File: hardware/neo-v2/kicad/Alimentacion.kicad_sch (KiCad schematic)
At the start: 64 parts, among them Q201 FS8205A, Q202 FS8205A, Q203 CSD25402Q3A, SW201 MSK-22D18G3, U201 TPS2121RUXR, U202 TPS61022RWUT, U203 BQ25170DSGR, U204 MAX17048G+T10, U205 DW01A

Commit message: NEO v2 fase 4: colocación y plan de layout
- PCB generado por script (tools/update_pcb.py) desde el PCB original de
  Nabu Casa y la netlist: contorno 84 x 89 mm con franja superior para
  batería y potencia, huellas retiradas y nuevas, zonas ampliadas,
  colocación de los bloques propios y de los puntos de prueba.
- Unión de fuentes rehecha: TPS2121 de entrada única abajo (sitio de U13)
  y LM66200 como diodo ideal en la franja, unidos por el plano +5V;
  elevador a 4,59 V. Cálculos actualizados.
- Retirados TP213 y TP221 (sin sitio); valor/DNP sincronizados.
- Huellas heredadas exportadas a kicad/lib/inherited (ERC sin avisos de
  enlace de huella).
- Paridad PCB/esquemático sin incidencias; DRC sin errores nuevos.
- docs/fase4-colocacion.md, renders, CHANGES y README.

Co-Authored-By: Claude Opus 5.5 <noreply@anthropic.com>
Claude-Session: https://claude.ai/code/session_01UWwWJAyCeb1aBHbGbkDaMx
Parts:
- removed R216, R218: 100k, Resistor_SMD:R_0402_1005Metric, symbol Device:R
- removed R217: 36.5k, Resistor_SMD:R_0402_1005Metric, symbol Device:R
- removed R219: 31.6k, Resistor_SMD:R_0402_1005Metric, symbol Device:R
- removed R223: 10k, Resistor_SMD:R_0402_1005Metric, symbol Device:R
- removed R224: 2.2M, Resistor_SMD:R_0402_1005Metric, symbol Device:R
- removed TP212: MUX_ST, TestPoint:TestPoint_Pad_D1.0mm, symbol Connector:TestPoint
- removed TP213: MUX_OV1, TestPoint:TestPoint_Pad_D1.0mm, symbol Connector:TestPoint
- added C218: 22uF 25V, Capacitor_SMD:C_0805_2012Metric, symbol Device:C
- added C219: 100nF, Capacitor_SMD:C_0402_1005Metric, symbol Device:C
- added U206: LM66200DRLR, Package_TO_SOT_SMD:SOT-583-8, symbol NEO_v2:LM66200
- R209: value 732k -> 665k; LCSC C27016 -> C56583
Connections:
- net MUX_CP2 is gone; now on net GND: U201.3 (CP2)
- net MUX_PR1 is gone; now on net GND: U201.6 (PR1)
- net +5V: now also C218.1, C219.1, U206.2 (VOUT), U206.7 (VOUT)
- net BOOST_5V: now also U206.3 (VIN1); no longer U201.2 (IN2)
- net GND: now also U201.2 (IN2), C218.2, C219.2, U206.1 (GND), U206.4 (~{ON}), U206.5 (GND), U206.6 (VIN2)
- net MUX_ST: no longer names the net of U201.9 (ST)
- no-connect marks 2 -> 4
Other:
- note added: "ELEVADOR TPS61022 (SLVSDX7D, fase 2 §4.2) VOUT = 0,6 V x (1 + 665k/100k) = 4,59 V (fase 4: por debajo de USB para el diodo ideal U206). MODE alto = PWM forzado (R211 0 Ohm; R212 DNP = PFM). L201 1 uH: IL pico 5,26 A a 2,7 V y 2 A < Isat 12 A; valle 3,44 A < ILIM mín. 6,5 A. COUT 3x22 uF (~30 uF efectivos): eq. 8 pide 21,6 uF para 50 mV pp. R214: puente 1206 de 0 Ohm; huella prevista para ferrita 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"
- note added: "UNIÓN DE FUENTES (fase 4, docs/fase4-colocacion.md §2). Sustituye al multiplexor único de la fase 2: entre la franja (batería) y el sitio de U13 (USB) no cabe una pista de 1,5-2 A en la placa heredada. U201 abajo: VBUS -> +5V, ILIM 44,2 k (2,0-3,0 A), OV1 43,2k/10k (5,64 V), SS 100 nF. Entrada única. U206 arriba: BOOST_5V (4,59 V) -> +5V. Con USB, +5V (~4,8-5,0 V) > BOOST_5V + 70 mV: bloquea. Sin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"
- note removed: "ELEVADOR TPS61022 (SLVSDX7D, fase 2 §4.2) VOUT = 0,6 V x (1 + 732k/100k) = 4,992 V. MODE alto = PWM forzado (R211 0 Ohm; R212 DNP = PFM). L201 1 uH: IL pico 5,26 A a 2,7 V y 2 A < Isat 12 A; valle 3,44 A < ILIM mín. 6,5 A. COUT 3x22 uF (~30 uF efectivos): eq. 8 pide 21,6 uF para 50 mV pp. R214: puente 1206 de 0 Ohm; huella prevista para ferrita si la medida lo pide. INTERRUPTOR SW201 (señal): OFF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"
- note removed: "MULTIPLEXOR TPS2121 (SLVSEA3F, fase 2 §4.1). Sustituye a U13 (SGM2594B). Modo XREF: IN1 (VBUS) si PR1 > CP2. CP2 = 4,992 x 31,6/131,6 = 1,199 V (> VREF máx. 1,10 V). PR1 100k/36,5k + 2,2 M desde ST: a batería con VBUS < 4,39 V, vuelve con VBUS > 4,54 V. OV1 43,2k/10k: corte a 5,64 V. ILIM 44,2 k: 2,0-3,0 A. SS 100 nF: 780 V/s. Error evitado: PR1 y CP2 con el mismo divisor = VBUS frente a VBOOST, 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"
- note removed: "PWR_FLAG de GND y +3V3: en las bibliotecas de Seeed la fuente de estos carriles es un pin pasivo (conector USB, bobina del buck), así que el ERC no sabe que están alimentados. No cambian ninguna neta. Los demás carriles heredados se marcan en su propia hoja (fase 5): KiCad no cuenta un PWR_FLAG como conexión si en la hoja no hay otro pin real del carril."

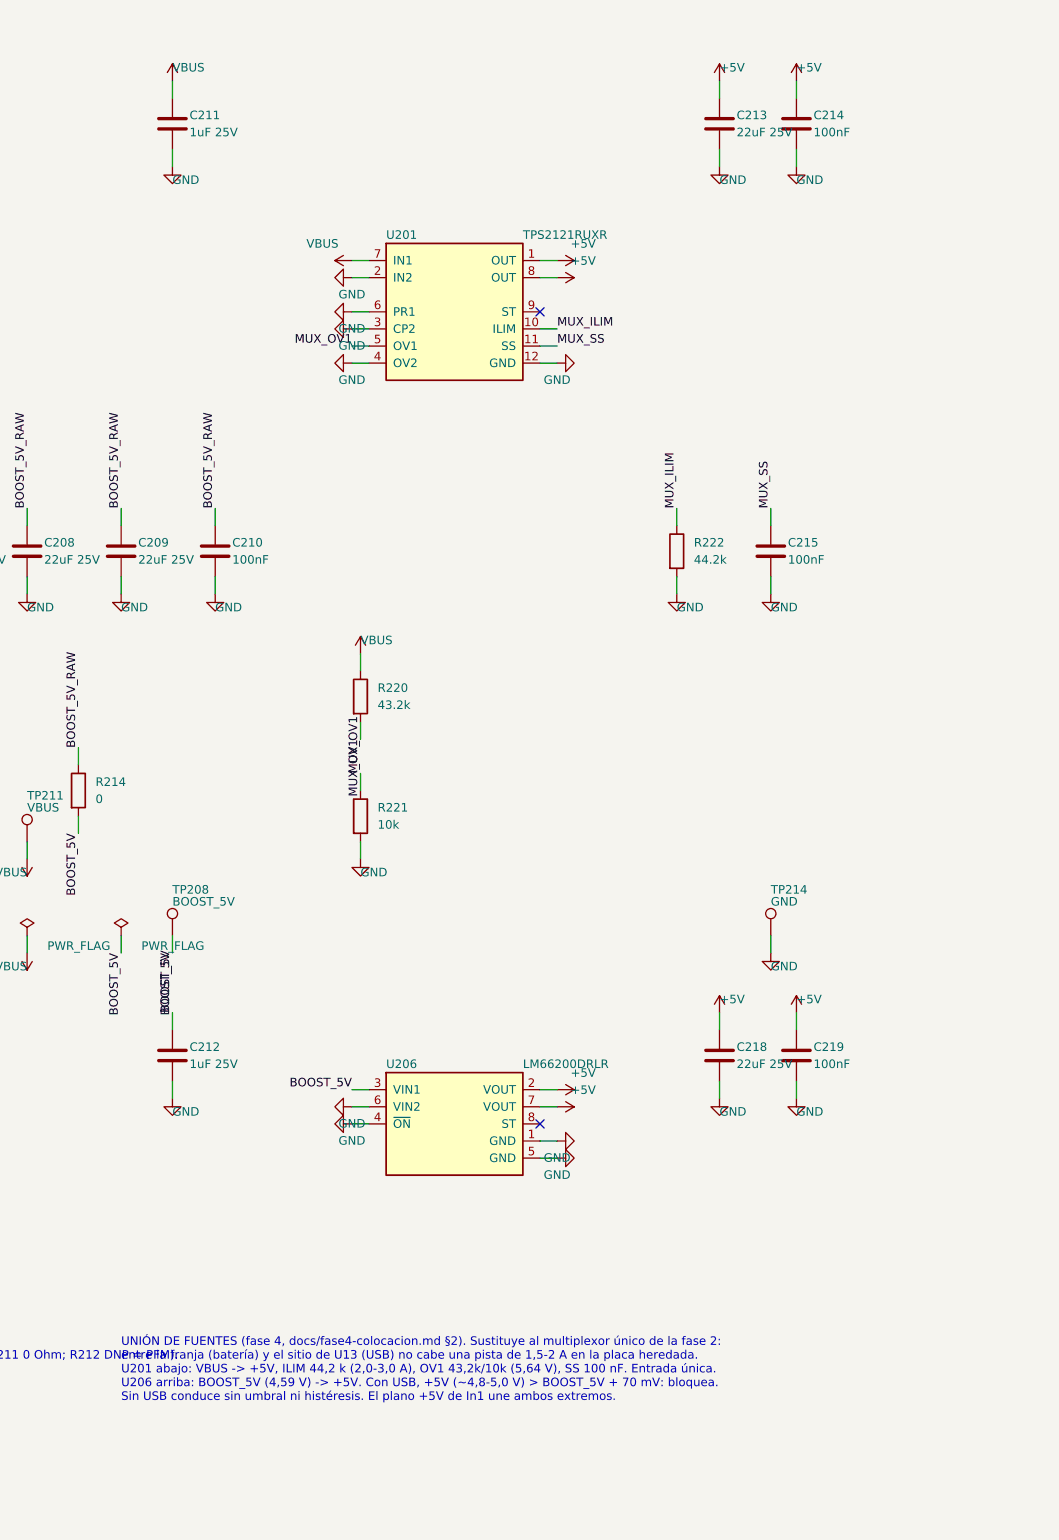
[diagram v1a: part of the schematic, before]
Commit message: NEO v2 fase 5: ruteo completo, ERC y DRC sin errores
- Router A* propio (tools/route_signals.py) en lugar de Freerouting, que
  no convergía y no garantiza respetar el cobre heredado: 71 conexiones,
  ~1225 mm y 56 vías nuevas, sin tocar cobre existente.
- Potencia y lazos críticos a mano (route_power.py); elevador recolocado
  con COUT junto a VOUT/GND; escapes de U201 y U203 reordenados.
- Cosido de GND en la franja y unión de bolsas aisladas (stitch_gnd.py).
- Retiradas R220 (OVP de U201: sin camino en el PCB heredado; protección
  igual que el original) y C214 (redundante con C83).
- ERC: 0 errores (anotaciones PWR_FLAG/no conexión en hojas heredadas).
- DRC con paridad: 0 violaciones, 0 pendientes; 8 errores del original
  como exclusiones comentadas (drc_exclusions.py).
- build_pcb.sh reconstruye el PCB de forma reproducible desde el original.
- docs/fase5-ruteo.md, renders, BOM de bloques nuevos, cálculos, CHANGES.

Co-Authored-By: Claude Opus 5.5 <noreply@anthropic.com>
Claude-Session: https://claude.ai/code/session_01UWwWJAyCeb1aBHbGbkDaMx
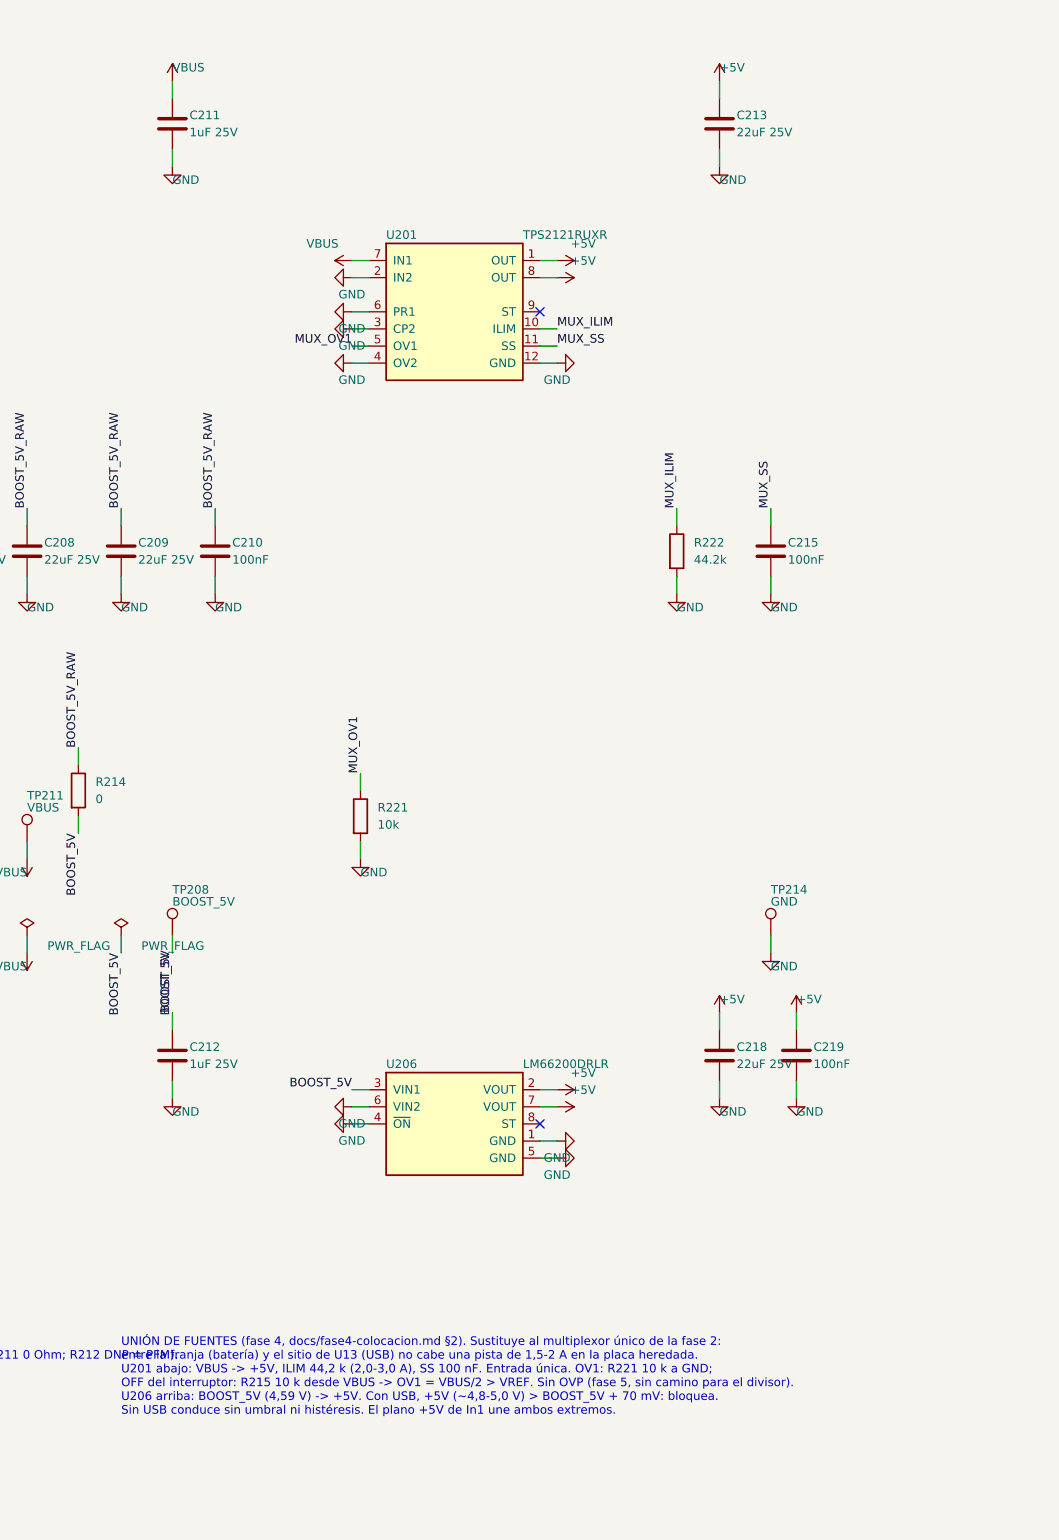
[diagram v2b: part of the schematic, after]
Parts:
- removed C214: 100nF, Capacitor_SMD:C_0402_1005Metric, symbol Device:C
- removed R220: 43.2k, Resistor_SMD:R_0402_1005Metric, symbol Device:R
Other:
- note added: "UNIÓN DE FUENTES (fase 4, docs/fase4-colocacion.md §2). Sustituye al multiplexor único de la fase 2: entre la franja (batería) y el sitio de U13 (USB) no cabe una pista de 1,5-2 A en la placa heredada. U201 abajo: VBUS -> +5V, ILIM 44,2 k (2,0-3,0 A), SS 100 nF. Entrada única. OV1: R221 10 k a GND; OFF del interruptor: R215 10 k desde VBUS -> OV1 = VBUS/2 > VREF. Sin OVP (fase 5, sin camino para 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"
- note removed: "UNIÓN DE FUENTES (fase 4, docs/fase4-colocacion.md §2). Sustituye al multiplexor único de la fase 2: entre la franja (batería) y el sitio de U13 (USB) no cabe una pista de 1,5-2 A en la placa heredada. U201 abajo: VBUS -> +5V, ILIM 44,2 k (2,0-3,0 A), OV1 43,2k/10k (5,64 V), SS 100 nF. Entrada única. U206 arriba: BOOST_5V (4,59 V) -> +5V. Con USB, +5V (~4,8-5,0 V) > BOOST_5V + 70 mV: bloquea. Sin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"
